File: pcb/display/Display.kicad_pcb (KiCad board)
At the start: 2 copper layers, 100 x 75 mm, 186 parts, among them J101 RJ45, J102 Screw Terminal 3.5mm, J103 01x08_Pin, J201 Term 3.5mm, J202 Term 3.5mm, J401 XH 2P, J402 XH 2P, J403 XH 2P, J404 XH 2P, J405 XH 2P, J406 XH 2P, J407 XH 2P, J501 XH 2P, J502 XH 2P, J503 XH 2P, J504 XH 2P, J505 XH 2P, J506 XH 2P, J507 XH 2P, P101 USB_C_Plug_USB2.0, Q101 2N7002, Q201 DOZ35N06, Q202 DOZ35N06, Q401 DOZ35N06, Q402 DOZ35N06, Q403 DOZ35N06, Q404 DOZ35N06, Q405 DOZ35N06, Q406 DOZ35N06, Q407 DOZ35N06, Q501 DOZ35N06, Q502 DOZ35N06, Q503 DOZ35N06, Q504 DOZ35N06, Q505 DOZ35N06, Q506 DOZ35N06, Q507 DOZ35N06, Q601 DOZ35N06, Q602 DOZ35N06, SW101 SW_4x3mm, SW102 SW_4x3mm, SW103 SW_4x3mm, SW104 SW_4x3mm, U101 TMP1075DSGR, U102 ESP32-S3-MINI-1U-N8, U201 PCA9685BS, U301 SP3485EN-L/TR, U302 E220-400M22S, U601 SIC438BED-T1-GE3, U602 TPS259474ARPWR, U603 TPS54202DDC, U604 TPS54202DDC, U605 LM74700, U606 LM74700

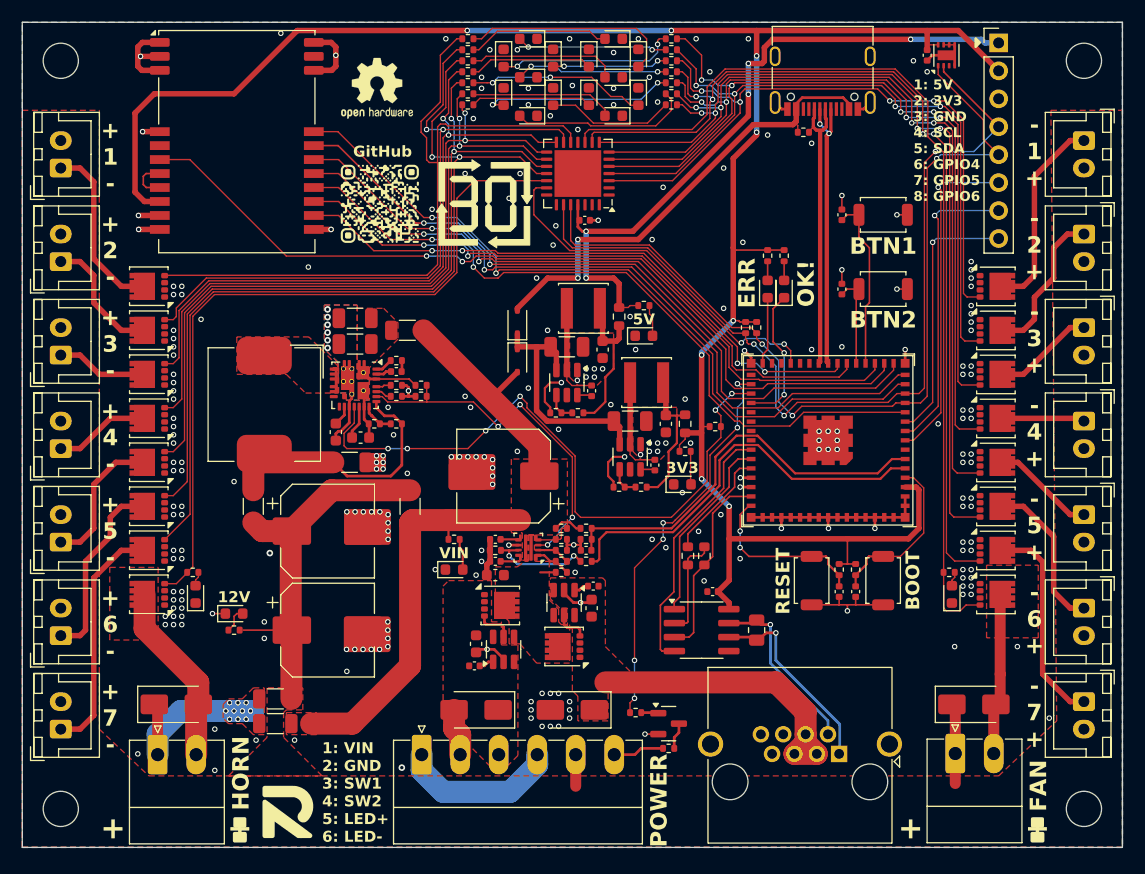
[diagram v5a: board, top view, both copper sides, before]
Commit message: OSC Display Hardware Revision 02
There might still be some errors which need to be corrected during ordering.
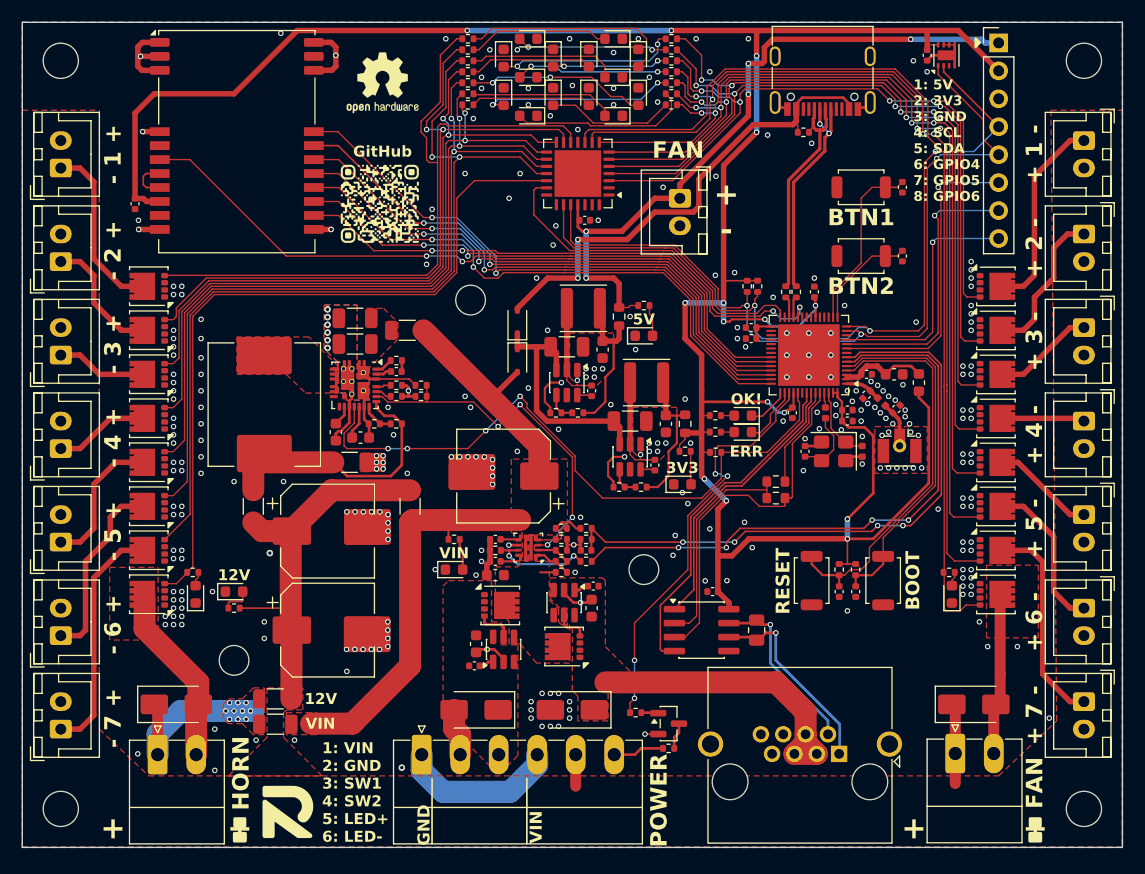
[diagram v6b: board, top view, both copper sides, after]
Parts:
- removed REF**: OSHW-Logo2_7.3x6mm_SilkScreen, Symbol:OSHW-Logo2_7.3x6mm_SilkScreen
- removed REF**: OpenShotClock, RVNSPRK_Logo:OpenShotClock
- removed REF**: KiCad-Logo2_5mm_SilkScreen, Symbol:KiCad-Logo2_5mm_SilkScreen
- added C1: 10u, Capacitor_SMD:C_0603_1608Metric, F.Cu at (129.2, 82.0)
- added C106: 1u, Capacitor_SMD:C_0402_1005Metric, F.Cu at (126.8, 82.0)
- added C107: 100n, Capacitor_SMD:C_0402_1005Metric, F.Cu at (120.0, 85.5)
- added C108: 100n, Capacitor_SMD:C_0402_1005Metric, F.Cu at (125.0, 85.3)
- added C109: 100n, Capacitor_SMD:C_0402_1005Metric, F.Cu at (122.0, 74.5)
- added C110: 1u, Capacitor_SMD:C_0402_1005Metric, F.Cu at (125.0, 86.3)
- added C111: 1.8pF, Capacitor_SMD:C_0402_1005Metric, F.Cu at (126.8, 83.8)
- added C112: 1.8pF, Capacitor_SMD:C_0402_1005Metric, F.Cu at (129.4, 85.2)
- added C113: 100n, Capacitor_SMD:C_0402_1005Metric, F.Cu at (116.2, 77.8)
- added C2: 12p, Capacitor_SMD:C_0402_1005Metric, F.Cu at (121.2, 89.0)
- added C3: 12p, Capacitor_SMD:C_0402_1005Metric, F.Cu at (126.3, 89.0)
- added C4: 1u, Capacitor_SMD:C_0402_1005Metric, F.Cu at (116.2, 78.8)
- added C5: 1u, Capacitor_SMD:C_0402_1005Metric, F.Cu at (60.2, 66.5)
- added FB1: 100R, Inductor_SMD:L_0603_1608Metric, F.Cu at (131.5, 82.8)
- added H1: M2.5, MountingHole:MountingHole_2.7mm_M2.5_DIN965, F.Cu at (69.2, 108.0)
- added H2: M2.5, MountingHole:MountingHole_2.7mm_M2.5_DIN965, F.Cu at (106.5, 99.8)
- added H3: M2.5, MountingHole:MountingHole_2.7mm_M2.5_DIN965, F.Cu at (90.8, 75.2)
- added J1: XH 2P, Connector_JST:JST_XH_B2B-XH-A_1x02_P2.50mm_Vertical, F.Cu at (109.8, 66.0)
- added J105: U.FL, RVNSPRK_Connector:U.FL_Hirose_U.FL-R-SMT-1_Vertical, F.Cu at (129.8, 88.5)
- added L1: 24nH, Inductor_SMD:L_0402_1005Metric, F.Cu at (123.0, 85.5)
- added L101: 2.7nH, Inductor_SMD:L_0402_1005Metric, F.Cu at (128.1, 84.5)
- added R2: 22R, Resistor_SMD:R_0402_1005Metric, F.Cu at (119.4, 74.5)
- added R3: 22R, Resistor_SMD:R_0402_1005Metric, F.Cu at (120.3, 74.5)
- added SYM1: Logo_Open_Hardware_Small, Symbol:OSHW-Logo2_7.3x6mm_SilkScreen, F.Cu at (82.8, 55.5)
- added SYM2: Logo_Open_Hardware_Small, Symbol:KiCad-Logo2_5mm_SilkScreen, B.Cu at (99.8, 121.2)
- added Y101: 3225 40MHz 10ppm, Crystal:Crystal_SMD_3225-4Pin_3.2x2.5mm, F.Cu at (123.8, 89.0)
- C104: value 100n -> 1u
- L602, L603: value 33uH -> 22uH
- R106: value 1k8 -> 10k
- U102: value ESP32-S3-MINI-1U-N8 -> ESP32-S3FN8; footprint Espressif:ESP32-S3-MINI-1U -> Package_DFN_QFN:QFN-56-1EP_7x7mm_P0.4mm_EP5.6x5.6mm
- moved R102 16.7 mm to (113.0, 87.2), turned to 0 degrees
- moved R101 15.8 mm to (113.0, 85.8), turned to 0 degrees
- moved D102 13.2 mm to (115.5, 87.2), turned to 180 degrees
- moved D101 12.1 mm to (115.5, 85.8), turned to 180 degrees
- moved R302 10.5 mm to (118.5, 91.8), turned to 180 degrees
- moved R303 8.36 mm to (118.5, 93.2), turned to 180 degrees
- moved U102 7.95 mm to (121.5, 80.2)
- moved C102 6.26 mm to (130.0, 71.2), turned to -90 degrees
- moved C101 6.04 mm to (130.0, 65.0), turned to -90 degrees
- moved R108 3.90 mm to (116.8, 74.0)
- moved R107 3.85 mm to (115.9, 74.0)
- moved G*** 3.75 mm to (81.0, 121.5)
- moved SW102 3.61 mm to (126.2, 71.2), turned to 180 degrees
- moved SW101 3.20 mm to (126.2, 65.0), turned to 180 degrees
- moved R110 2.34 mm to (113.0, 89.1)
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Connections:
- C104 pad 1: Net-(U102-EN) -> /RESET
- J102 pad 1: Net-(J102-Pin_1) -> GND
- J102 pad 4: Net-(J102-Pin_1) -> GND
- R106 pad 2: Net-(U102-EN) -> /RESET
- SW103 pad 1: Net-(U102-EN) -> /RESET
- U102 pad 1: GND -> Net-(U102-LNA_IN/RF)
- U102 pad 10: /GPIOz -> /GPIOy
- U102 pad 11: /LORA.RST -> /GPIOz
- U102 pad 12: /I2C.SDA -> unconnected-(U102-GPIO7/ADC1_CH6-Pad12)
- U102 pad 13: /I2C.SCL -> /I2C.SDA
- U102 pad 14: /LORA.NSS -> /I2C.SCL
- U102 pad 15: /SPI.MOSI -> /BTN2
- U102 pad 16: /SPI.CLK -> /BTN1
- U102 pad 17: /SPI.MISO -> unconnected-(U102-GPIO12/ADC2_CH1-Pad17)
- U102 pad 18: /LORA.DIO1 -> unconnected-(U102-GPIO13/ADC2_CH2-Pad18)
- U102 pad 19: /BTN1 -> unconnected-(U102-GPIO14/ADC2_CH3-Pad19)
- U102 pad 2: GND -> +3.3VD
- U102 pad 20: /BTN2 -> +3.3V
- U102 pad 21: /LORA.BUSY -> unconnected-(U102-GPIO15/ADC2_CH4/XTAL_32K_P-Pad21)
- U102 pad 22: /LORA.IRQ -> unconnected-(U102-GPIO16/ADC2_CH5/XTAL_32K_N-Pad22)
- U102 pad 23: /D_N -> unconnected-(U102-GPIO17/ADC2_CH6-Pad23)
- U102 pad 24: /D_P -> /LORA.IRQ
- U102 pad 25: unconnected-(U102-GPIO21-Pad25) -> Net-(U102-GPIO19/USB_D-/ADC2_CH8)
- U102 pad 26: unconnected-(U102-GPIO26-Pad26) -> Net-(U102-GPIO20/USB_D+/ADC2_CH9)
- U102 pad 27: /PWM.OE -> unconnected-(U102-GPIO21-Pad27)
- U102 pad 28: unconnected-(U102-SPIIO4/GPIO33/FSPIHD/SUBSPIHD-Pad28) -> /PWM.OE
- U102 pad 29: unconnected-(U102-SPIIO5/GPIO34/FSPICS0/SUBSPICS0-Pad29) -> VSPI
- U102 pad 3: +3.3V -> +3.3VD
- U102 pad 30: /LED.ERR -> unconnected-(U102-SPIHD/GPIO27-Pad30)
- U102 pad 32: /LED.STATUS -> unconnected-(U102-SPICS0/GPIO29-Pad32)
- U102 pad 33: /12V_PG -> unconnected-(U102-SPICLK/GPIO30-Pad33)
- U102 pad 34: /LED.OK -> unconnected-(U102-SPIQ/GPIO31-Pad34)
- U102 pad 36: unconnected-(U102-MTDO/GPIO40/CLK_OUT2-Pad36) -> /LORA.BUSY
- U102 pad 37: unconnected-(U102-MTDI/GPIO41/CLK_OUT1-Pad37) -> /LORA.DIO1
- U102 pad 38: unconnected-(U102-MTMS/GPIO42-Pad38) -> /SPI.MISO
- U102 pad 39: /UART.TX -> /SPI.CLK
- U102 pad 4: /BOOT -> /RESET
- U102 pad 40: /UART.RX -> /SPI.MOSI
- U102 pad 41: /UART.~{RXEN} -> /LORA.NSS
- U102 pad 42: GND -> /LORA.RST
- U102 pad 43: GND -> /LED.OK
- U102 pad 44: /UART.TXEN -> /LED.ERR
- U102 pad 45: Net-(U102-EN) -> /LED.STATUS
- U102 pad 46: GND -> +3.3V
- U102 pad 47: GND -> /12V_PG
- U102 pad 48: GND -> unconnected-(U102-MTMS/JTAG/GPIO42-Pad48)
- U102 pad 49: GND -> /UART.TX
- U102 pad 5: /I_SENSE -> /BOOT
- U102 pad 50: GND -> /UART.RX
- U102 pad 51: GND -> /UART.~{RXEN}
- U102 pad 52: GND -> /UART.TXEN
- U102 pad 53: GND -> Net-(U102-XTAL_N)
- U102 pad 54: GND -> Net-(U102-XTAL_P)
- U102 pad 55: GND -> +3.3V
- U102 pad 56: GND -> +3.3V
- U102 pad 6: /V_SENSE -> /I_SENSE
- U102 pad 7: /FAN.PWM -> /V_SENSE
- U102 pad 8: /GPIOx -> unconnected-(U102-GPIO3/ADC1_CH2-Pad8)
- U102 pad 9: /GPIOy -> /GPIOx
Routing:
- net +3.3V: track 189.6 -> 239.2 mm, vias 8 -> 15
- net /RESET: track 0.00 -> 36.3 mm
- net GND: track 107.7 -> 84.7 mm, vias 258 -> 305
- net /V_SENSE: track 37.4 -> 57.1 mm, vias 0 -> 4
- net /I_SENSE: track 37.0 -> 54.7 mm, vias 0 -> 4
- net /BOOT: track 15.3 -> 32.5 mm
- net /UART.TXEN: track 17.6 -> 33.5 mm
- net Net-(U102-EN): track 15.7 -> 0.00 mm, vias 2 -> 0
- net /LORA.NSS: track 68.9 -> 53.9 mm
- net /SPI.MOSI: track 67.6 -> 52.7 mm
- net Net-(J102-Pin_1): track 14.7 -> 0.00 mm
- net /LORA.RST: track 66.7 -> 52.1 mm
- net /SPI.CLK: track 66.6 -> 52.5 mm
- net /SPI.MISO: track 63.7 -> 51.5 mm
- net Net-(U301-~{RE}): track 9.30 -> 20.1 mm
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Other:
- board text added: "+ -"
- board text added: "GND"
- board text added: "Rev. 02 яαvεηsραяκ 2026"
- board text removed: "Rev. 01 яαvεηsραяκ 2025"
